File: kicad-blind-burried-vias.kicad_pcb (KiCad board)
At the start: 6 copper layers, 62 x 53 mm, 2 parts

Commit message: Update
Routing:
- net /blind_vias_path: track 32.6 -> 39.6 mm
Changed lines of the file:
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@@
   )
   (gr_rect (start 121 70) (end 183 123) (layer "Edge.Cuts") (width 0.1) (fill none))
-  (segment (start 159.7 112.2) (end 162.4 112.2) (width 0.25) (layer "F.Cu") (net 1))
-  (segment (start 136.47 112.245) (end 144.055 112.245) (width 0.25) (layer "F.Cu") (net 1))
-  (segment (start 150.9 112.2) (end 156.3 112.2) (width 0.25) (layer "F.Cu") (net 1))
-  (segment (start 144.055 112.245) (end 144.1 112.2) (width 0.25) (layer "F.Cu") (net 1))
-  (via blind (at 162.4 112.2) (size 0.8) (drill 0.4) (layers "F.Cu" "B.Cu") (net 1))
-  (via blind (at 150.9 112.2) (size 0.8) (drill 0.4) (layers "F.Cu" "In1.Cu") (net 1))
-  (via blind (at 156.3 112.2) (size 0.8) (drill 0.4) (layers "F.Cu" "B.Cu") (net 1))
-  (via blind (at 159.7 112.2) (size 0.8) (drill 0.4) (layers "F.Cu" "In3.Cu") (net 1))
-  (via blind (at 144.1 112.2) (size 0.8) (drill 0.4) (layers "F.Cu" "B.Cu") (remove_unused_layers) (net 1))
-  (segment (start 144.1 112.2) (end 150.9 112.2) (width 0.25) (layer "In1.Cu") (net 1))
-  (segment (start 156.3 112.2) (end 159.7 112.2) (width 0.25) (layer "In3.Cu") (net 1))
-  (segment (start 162.4 112.2) (end 162.445 112.245) (width 0.25) (layer "B.Cu") (net 1))
-  (segment (start 162.445 112.245) (end 169 112.245) (width 0.25) (layer "B.Cu") (net 1))
+  (segment (start 152.6 112.2) (end 151.1 113.7) (width 0.25) (layer "F.Cu") (net 1))
+  (segment (start 145 110.5) (end 143.255 112.245) (width 0.25) (layer "F.Cu") (net 1))
+  (segment (start 156.6 110.5) (end 154.9 112.2) (width 0.25) (layer "F.Cu") (net 1))
+  (segment (start 143.255 112.245) (end 136.47 112.245) (width 0.25) (layer "F.Cu") (net 1))
+  (segment (start 160.2 111.4) (end 157.9 113.7) (width 0.25) (layer "F.Cu") (net 1))
+  (segment (start 163.2 111.4) (end 160.2 111.4) (width 0.25) (layer "F.Cu") (net 1))
+  (segment (start 154.9 112.2) (end 152.6 112.2) (width 0.25) (layer "F.Cu") (net 1))
+  (via blind (at 163.2 111.4) (size 0.8) (drill 0.4) (layers "F.Cu" "B.Cu") (net 1))
+  (via blind (at 151.1 113.7) (size 0.8) (drill 0.4) (layers "F.Cu" "In1.Cu") (net 1))
+  (via blind (at 156.6 110.5) (size 0.8) (drill 0.4) (layers "F.Cu" "B.Cu") (net 1))
+  (via blind (at 157.9 113.7) (size 0.8) (drill 0.4) (layers "F.Cu" "In3.Cu") (net 1))
+  (via blind (at 145 110.5) (size 0.8) (drill 0.4) (layers "F.Cu" "B.Cu") (remove_unused_layers) (net 1))
+  (segment (start 151.1 113.7) (end 149.6 112.2) (width 0.25) (layer "In1.Cu") (net 1))
+  (segment (start 146.7 112.2) (end 145 110.5) (width 0.25) (layer "In1.Cu") (net 1))
+  (segment (start 149.6 112.2) (end 146.7 112.2) (width 0.25) (layer "In1.Cu") (net 1))
+  (segment (start 157.9 113.7) (end 157.9 111.8) (width 0.25) (layer "In3.Cu") (net 1))
+  (segment (start 157.9 111.8) (end 156.6 110.5) (width 0.25) (layer "In3.Cu") (net 1))
+  (segment (start 164.045 112.245) (end 169 112.245) (width 0.25) (layer "B.Cu") (net 1))
+  (segment (start 163.2 111.4) (end 164.045 112.245) (width 0.25) (layer "B.Cu") (net 1))
   (segment (start 150.035 81.765) (end 169 81.765) (width 0.25) (layer "F.Cu") (net 2))
   (segment (start 149.9 81.9) (end 150.035 81.765) (width 0.25) (layer "F.Cu") (net 2))

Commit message: Update
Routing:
- net /burried_vias_path: track 32.6 -> 56.5 mm, vias 1 -> 2
- net /blind_vias_path: track 39.6 -> 32.6 mm, vias 5 -> 2
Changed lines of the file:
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@@
   )
   (gr_rect (start 121 70) (end 183 123) (layer "Edge.Cuts") (width 0.1) (fill none))
-  (segment (start 152.6 112.2) (end 151.1 113.7) (width 0.25) (layer "F.Cu") (net 1))
-  (segment (start 145 110.5) (end 143.255 112.245) (width 0.25) (layer "F.Cu") (net 1))
-  (segment (start 156.6 110.5) (end 154.9 112.2) (width 0.25) (layer "F.Cu") (net 1))
-  (segment (start 143.255 112.245) (end 136.47 112.245) (width 0.25) (layer "F.Cu") (net 1))
-  (segment (start 160.2 111.4) (end 157.9 113.7) (width 0.25) (layer "F.Cu") (net 1))
-  (segment (start 163.2 111.4) (end 160.2 111.4) (width 0.25) (layer "F.Cu") (net 1))
-  (segment (start 154.9 112.2) (end 152.6 112.2) (width 0.25) (layer "F.Cu") (net 1))
-  (via blind (at 163.2 111.4) (size 0.8) (drill 0.4) (layers "F.Cu" "B.Cu") (net 1))
-  (via blind (at 151.1 113.7) (size 0.8) (drill 0.4) (layers "F.Cu" "In1.Cu") (net 1))
-  (via blind (at 156.6 110.5) (size 0.8) (drill 0.4) (layers "F.Cu" "B.Cu") (net 1))
-  (via blind (at 157.9 113.7) (size 0.8) (drill 0.4) (layers "F.Cu" "In3.Cu") (net 1))
-  (via blind (at 145 110.5) (size 0.8) (drill 0.4) (layers "F.Cu" "B.Cu") (remove_unused_layers) (net 1))
-  (segment (start 151.1 113.7) (end 149.6 112.2) (width 0.25) (layer "In1.Cu") (net 1))
-  (segment (start 146.7 112.2) (end 145 110.5) (width 0.25) (layer "In1.Cu") (net 1))
-  (segment (start 149.6 112.2) (end 146.7 112.2) (width 0.25) (layer "In1.Cu") (net 1))
-  (segment (start 157.9 113.7) (end 157.9 111.8) (width 0.25) (layer "In3.Cu") (net 1))
-  (segment (start 157.9 111.8) (end 156.6 110.5) (width 0.25) (layer "In3.Cu") (net 1))
-  (segment (start 164.045 112.245) (end 169 112.245) (width 0.25) (layer "B.Cu") (net 1))
-  (segment (start 163.2 111.4) (end 164.045 112.245) (width 0.25) (layer "B.Cu") (net 1))
-  (segment (start 150.035 81.765) (end 169 81.765) (width 0.25) (layer "F.Cu") (net 2))
+  (segment (start 148.2 112.2) (end 148.155 112.245) (width 0.25) (layer "In1.Cu") (net 1))
+  (segment (start 136.47 112.245) (end 148.155 112.245) (width 0.25) (layer "In1.Cu") (net 1))
+  (segment (start 159.645 112.245) (end 169 112.245) (width 0.25) (layer "In1.Cu") (net 1))
+  (segment (start 159.6 112.2) (end 159.645 112.245) (width 0.25) (layer "In1.Cu") (net 1))
+  (via blind (at 159.6 112.2) (size 0.8) (drill 0.4) (layers "In1.Cu" "In2.Cu") (remove_unused_layers) (net 1))
+  (via blind (at 148.155 112.245) (size 0.8) (drill 0.4) (layers "In1.Cu" "In2.Cu") (remove_unused_layers) (net 1))
+  (segment (start 148.155 112.245) (end 159.555 112.245) (width 0.25) (layer "In2.Cu") (net 1))
+  (segment (start 159.555 112.245) (end 159.6 112.2) (width 0.25) (layer "In3.Cu") (net 1))
+  (segment (start 150.035 81.765) (end 161.165 81.765) (width 0.25) (layer "F.Cu") (net 2))
+  (segment (start 149.9 86.3) (end 158.8 86.3) (width 0.25) (layer "F.Cu") (net 2))
+  (segment (start 161.165 81.765) (end 169 81.765) (width 0.25) (layer "F.Cu") (net 2))
+  (segment (start 158.8 86.3) (end 161.165 83.935) (width 0.25) (layer "F.Cu") (net 2))
   (segment (start 149.9 81.9) (end 150.035 81.765) (width 0.25) (layer "F.Cu") (net 2))
+  (segment (start 161.165 83.935) (end 161.165 81.765) (width 0.25) (layer "F.Cu") (net 2))
   (via blind (at 149.9 81.9) (size 0.8) (drill 0.4) (layers "F.Cu" "B.Cu") (net 2))
-  (segment (start 136.47 81.765) (end 149.765 81.765) (width 0.25) (layer "B.Cu") (net 2))
+  (via (at 149.9 86.3) (size 0.8) (drill 0.4) (layers "F.Cu" "B.Cu") (net 2))
+  (segment (start 146.2 86.4) (end 149.8 86.4) (width 0.25) (layer "B.Cu") (net 2))
+  (segment (start 136.47 81.765) (end 143.535 81.765) (width 0.25) (layer "B.Cu") (net 2))
+  (segment (start 143.535 81.765) (end 149.765 81.765) (width 0.25) (layer "B.Cu") (net 2))
+  (segment (start 149.8 86.4) (end 149.9 86.3) (width 0.25) (layer "B.Cu") (net 2))
+  (segment (start 143.535 81.765) (end 143.535 83.735) (width 0.25) (layer "B.Cu") (net 2))
+  (segment (start 143.535 83.735) (end 146.2 86.4) (width 0.25) (layer "B.Cu") (net 2))
   (segment (start 149.765 81.765) (end 149.9 81.9) (width 0.25) (layer "B.Cu") (net 2))
 )

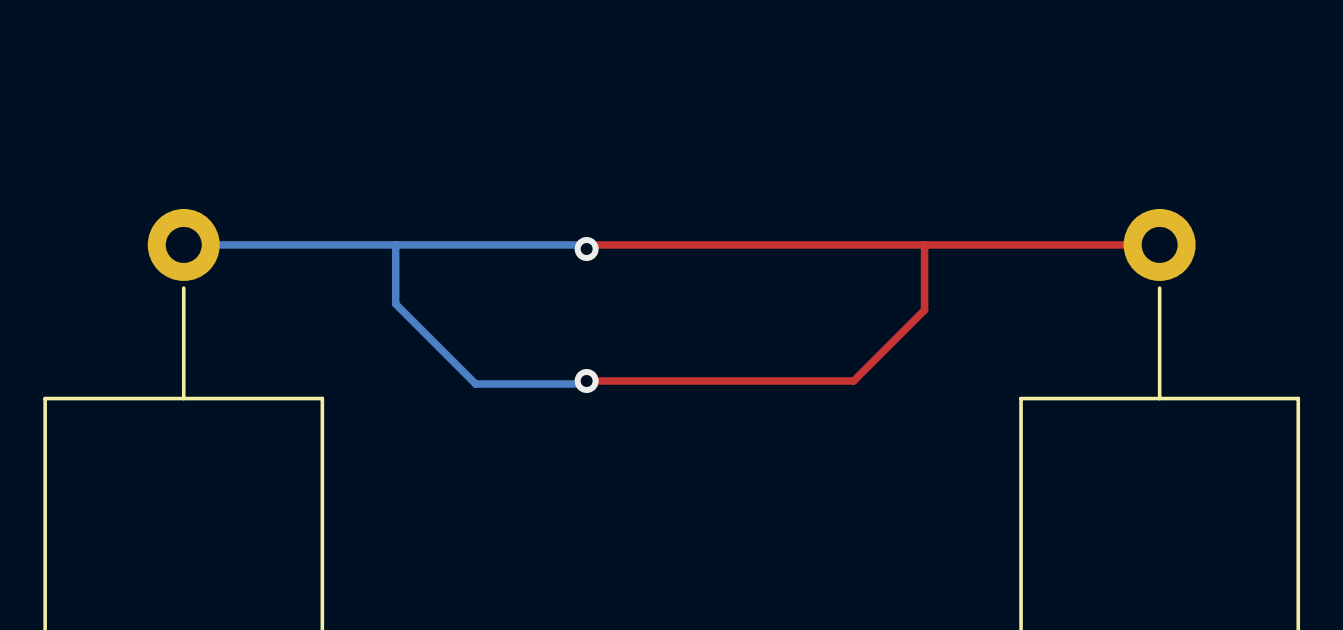
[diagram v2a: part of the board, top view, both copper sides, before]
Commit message: Remove vias and routing
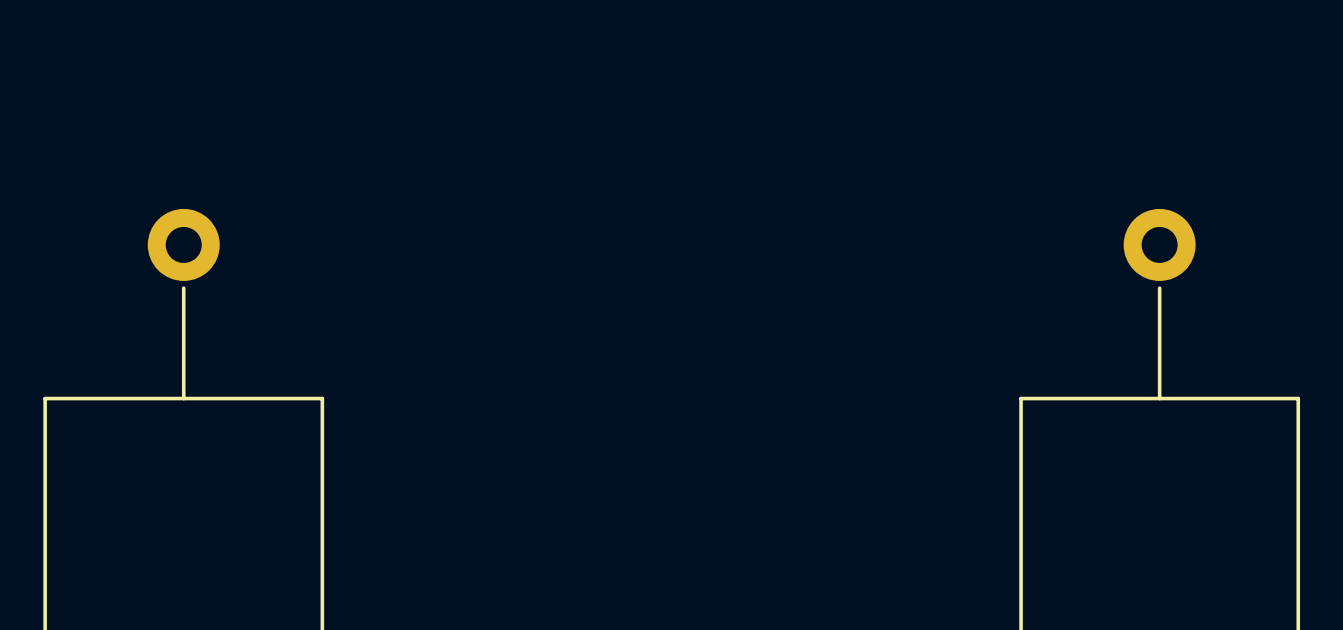
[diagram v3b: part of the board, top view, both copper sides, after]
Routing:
- net /burried_vias_path: track 56.5 -> 0.00 mm, vias 2 -> 0
- net /blind_vias_path: track 32.6 -> 0.00 mm, vias 2 -> 0
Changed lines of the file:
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@@
   )
   (gr_rect (start 121 70) (end 183 123) (layer "Edge.Cuts") (width 0.1) (fill none))
-  (segment (start 148.2 112.2) (end 148.155 112.245) (width 0.25) (layer "In1.Cu") (net 1))
-  (segment (start 136.47 112.245) (end 148.155 112.245) (width 0.25) (layer "In1.Cu") (net 1))
-  (segment (start 159.645 112.245) (end 169 112.245) (width 0.25) (layer "In1.Cu") (net 1))
-  (segment (start 159.6 112.2) (end 159.645 112.245) (width 0.25) (layer "In1.Cu") (net 1))
-  (via blind (at 159.6 112.2) (size 0.8) (drill 0.4) (layers "In1.Cu" "In2.Cu") (remove_unused_layers) (net 1))
-  (via blind (at 148.155 112.245) (size 0.8) (drill 0.4) (layers "In1.Cu" "In2.Cu") (remove_unused_layers) (net 1))
-  (segment (start 148.155 112.245) (end 159.555 112.245) (width 0.25) (layer "In2.Cu") (net 1))
-  (segment (start 159.555 112.245) (end 159.6 112.2) (width 0.25) (layer "In3.Cu") (net 1))
-  (segment (start 150.035 81.765) (end 161.165 81.765) (width 0.25) (layer "F.Cu") (net 2))
-  (segment (start 149.9 86.3) (end 158.8 86.3) (width 0.25) (layer "F.Cu") (net 2))
-  (segment (start 161.165 81.765) (end 169 81.765) (width 0.25) (layer "F.Cu") (net 2))
-  (segment (start 158.8 86.3) (end 161.165 83.935) (width 0.25) (layer "F.Cu") (net 2))
-  (segment (start 149.9 81.9) (end 150.035 81.765) (width 0.25) (layer "F.Cu") (net 2))
-  (segment (start 161.165 83.935) (end 161.165 81.765) (width 0.25) (layer "F.Cu") (net 2))
-  (via blind (at 149.9 81.9) (size 0.8) (drill 0.4) (layers "F.Cu" "B.Cu") (net 2))
-  (via (at 149.9 86.3) (size 0.8) (drill 0.4) (layers "F.Cu" "B.Cu") (net 2))
-  (segment (start 146.2 86.4) (end 149.8 86.4) (width 0.25) (layer "B.Cu") (net 2))
-  (segment (start 136.47 81.765) (end 143.535 81.765) (width 0.25) (layer "B.Cu") (net 2))
-  (segment (start 143.535 81.765) (end 149.765 81.765) (width 0.25) (layer "B.Cu") (net 2))
-  (segment (start 149.8 86.4) (end 149.9 86.3) (width 0.25) (layer "B.Cu") (net 2))
-  (segment (start 143.535 81.765) (end 143.535 83.735) (width 0.25) (layer "B.Cu") (net 2))
-  (segment (start 143.535 83.735) (end 146.2 86.4) (width 0.25) (layer "B.Cu") (net 2))
-  (segment (start 149.765 81.765) (end 149.9 81.9) (width 0.25) (layer "B.Cu") (net 2))
 )

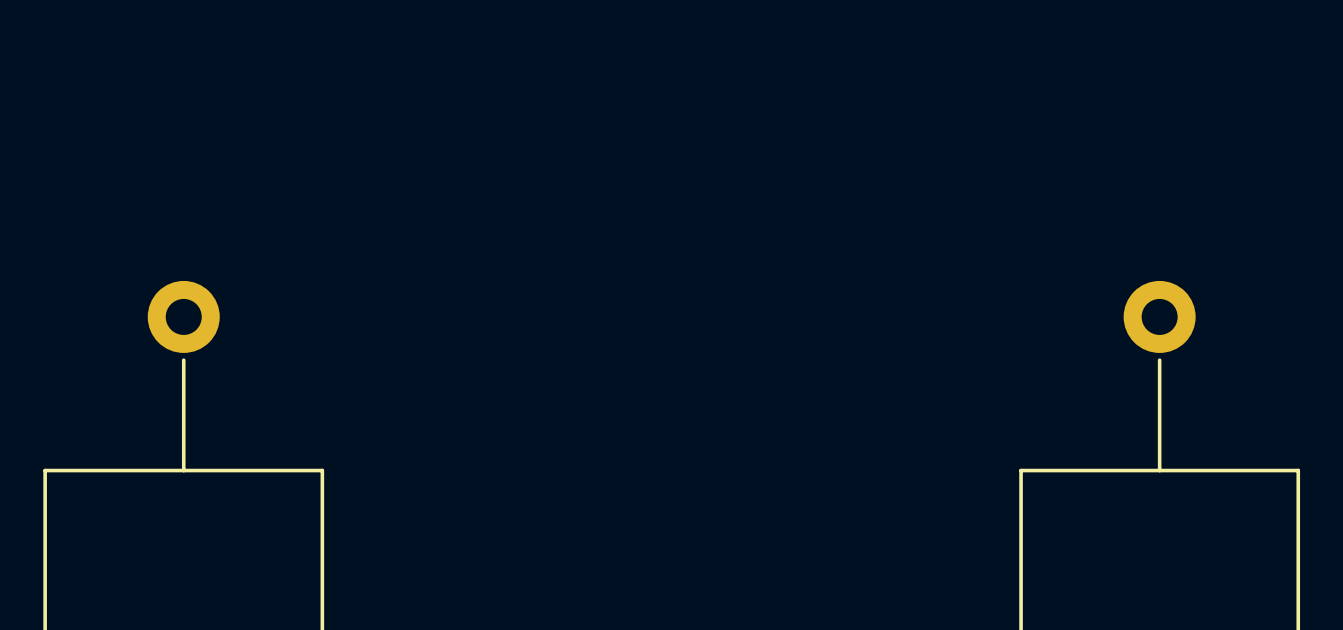
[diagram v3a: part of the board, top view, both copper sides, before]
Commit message: Add normal VIA
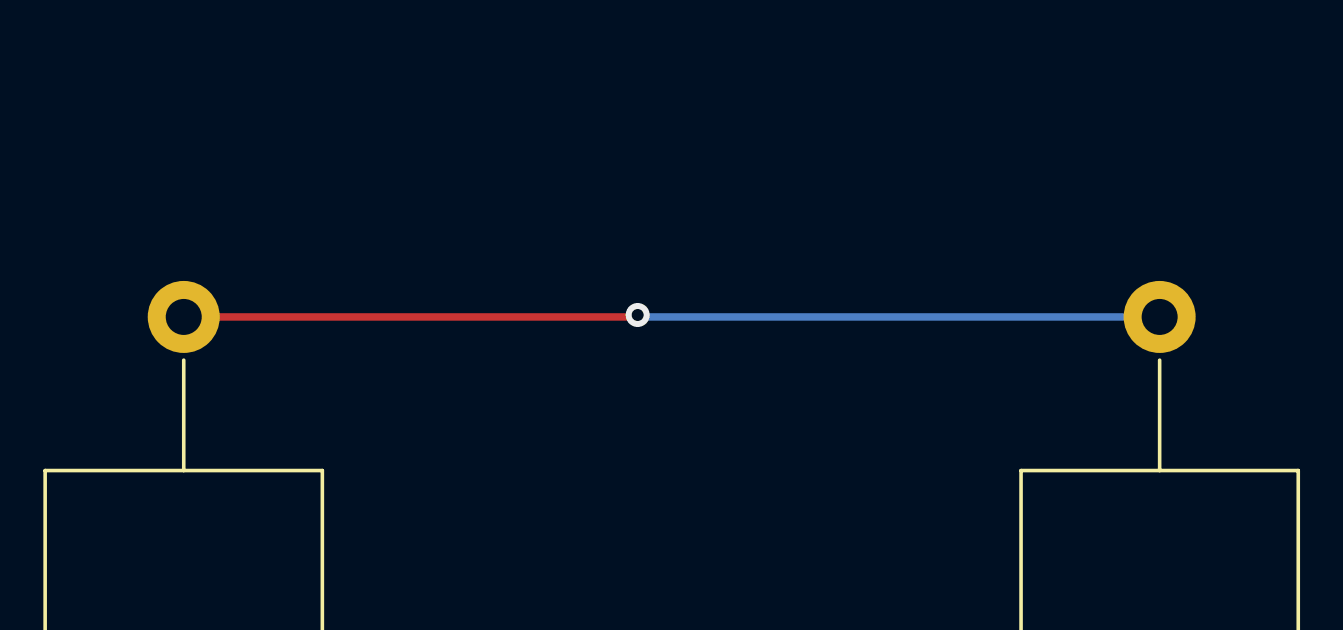
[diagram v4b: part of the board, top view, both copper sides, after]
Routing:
- net /burried_vias_path: track 0.00 -> 32.6 mm, vias 0 -> 1
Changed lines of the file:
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@@
   )
   (gr_rect (start 121 70) (end 183 123) (layer "Edge.Cuts") (width 0.1) (fill none))
+  (segment (start 136.47 81.765) (end 151.535 81.765) (width 0.25) (layer "F.Cu") (net 2))
+  (segment (start 151.535 81.765) (end 151.6 81.7) (width 0.25) (layer "F.Cu") (net 2))
+  (via (at 151.6 81.7) (size 0.8) (drill 0.4) (layers "F.Cu" "B.Cu") (net 2))
+  (segment (start 151.665 81.765) (end 169 81.765) (width 0.25) (layer "B.Cu") (net 2))
+  (segment (start 151.6 81.7) (end 151.665 81.765) (width 0.25) (layer "B.Cu") (net 2))
 )

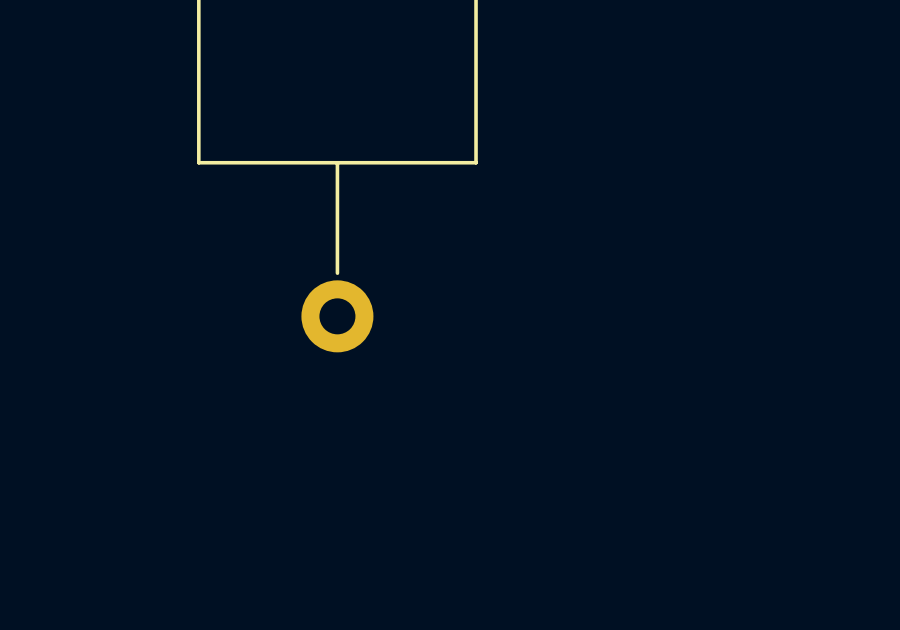
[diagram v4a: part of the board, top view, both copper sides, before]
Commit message: Add blind VIA (F.Cu-In1.CU)
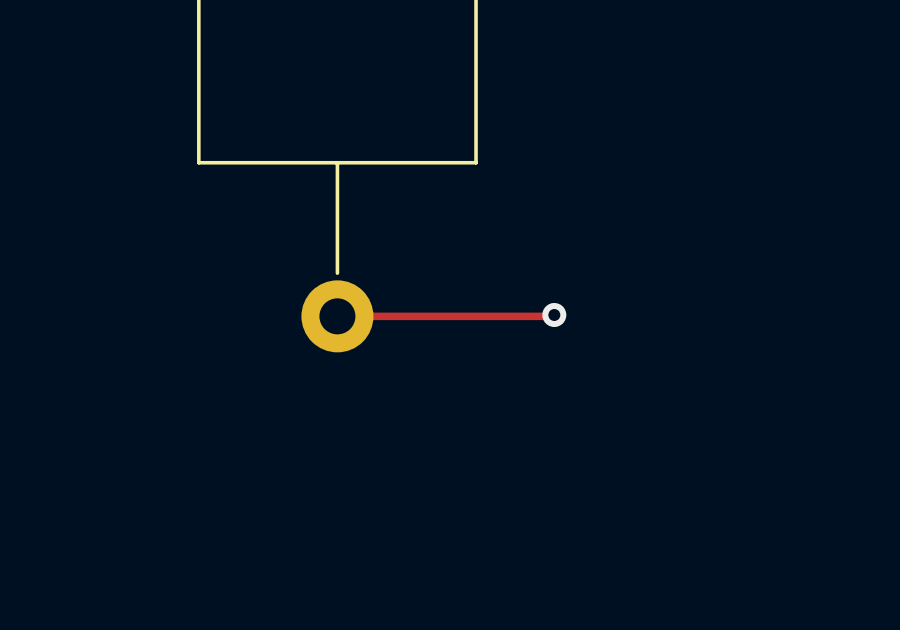
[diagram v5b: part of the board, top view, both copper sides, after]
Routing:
- net /blind_vias_path: track 0.00 -> 32.6 mm, vias 0 -> 1
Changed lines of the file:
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@@
   )
   (gr_rect (start 121 70) (end 183 123) (layer "Edge.Cuts") (width 0.1) (fill none))
+  (segment (start 136.47 112.245) (end 143.655 112.245) (width 0.25) (layer "F.Cu") (net 1))
+  (segment (start 143.655 112.245) (end 143.7 112.2) (width 0.25) (layer "F.Cu") (net 1))
+  (via blind (at 143.7 112.2) (size 0.8) (drill 0.4) (layers "F.Cu" "In1.Cu") (net 1))
+  (segment (start 143.7 112.2) (end 143.745 112.245) (width 0.25) (layer "In1.Cu") (net 1))
+  (segment (start 143.745 112.245) (end 169 112.245) (width 0.25) (layer "In1.Cu") (net 1))
   (segment (start 136.47 81.765) (end 151.535 81.765) (width 0.25) (layer "F.Cu") (net 2))
   (segment (start 151.535 81.765) (end 151.6 81.7) (width 0.25) (layer "F.Cu") (net 2))

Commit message: Add burried VIA (In1.Cu-In2.CU)
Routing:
- net /blind_vias_path: track 32.6 -> 52.4 mm, vias 1 -> 2
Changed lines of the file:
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@@
   (segment (start 143.655 112.245) (end 143.7 112.2) (width 0.25) (layer "F.Cu") (net 1))
   (via blind (at 143.7 112.2) (size 0.8) (drill 0.4) (layers "F.Cu" "In1.Cu") (net 1))
+  (segment (start 153.345 112.245) (end 153.6 111.99) (width 0.25) (layer "In1.Cu") (net 1))
   (segment (start 143.7 112.2) (end 143.745 112.245) (width 0.25) (layer "In1.Cu") (net 1))
-  (segment (start 143.745 112.245) (end 169 112.245) (width 0.25) (layer "In1.Cu") (net 1))
+  (segment (start 153.345 112.245) (end 169 112.245) (width 0.25) (layer "In1.Cu") (net 1))
+  (segment (start 143.745 112.245) (end 153.345 112.245) (width 0.25) (layer "In1.Cu") (net 1))
+  (segment (start 153.6 111.99) (end 153.6 109.2) (width 0.25) (layer "In1.Cu") (net 1))
+  (via blind (at 153.6 109.2) (size 0.8) (drill 0.4) (layers "In1.Cu" "In2.Cu") (net 1))
+  (segment (start 165.955 109.2) (end 169 112.245) (width 0.25) (layer "In2.Cu") (net 1))
+  (segment (start 153.6 109.2) (end 165.955 109.2) (width 0.25) (layer "In2.Cu") (net 1))
   (segment (start 136.47 81.765) (end 151.535 81.765) (width 0.25) (layer "F.Cu") (net 2))
   (segment (start 151.535 81.765) (end 151.6 81.7) (width 0.25) (layer "F.Cu") (net 2))
